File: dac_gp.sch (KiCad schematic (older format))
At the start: 47 parts, among them U1 DAC80508ZRTER, U2 OPA2156xD, U26 OPA2156xD, U27 OPA2156xD, U28 OPA2156xD, U3 OPA2156xD, U4 OPA2156xD, U6 OPA2156xD, U7 TMUX6136PWR, U8 OPA2156xD, U9 TMUX6136PWR

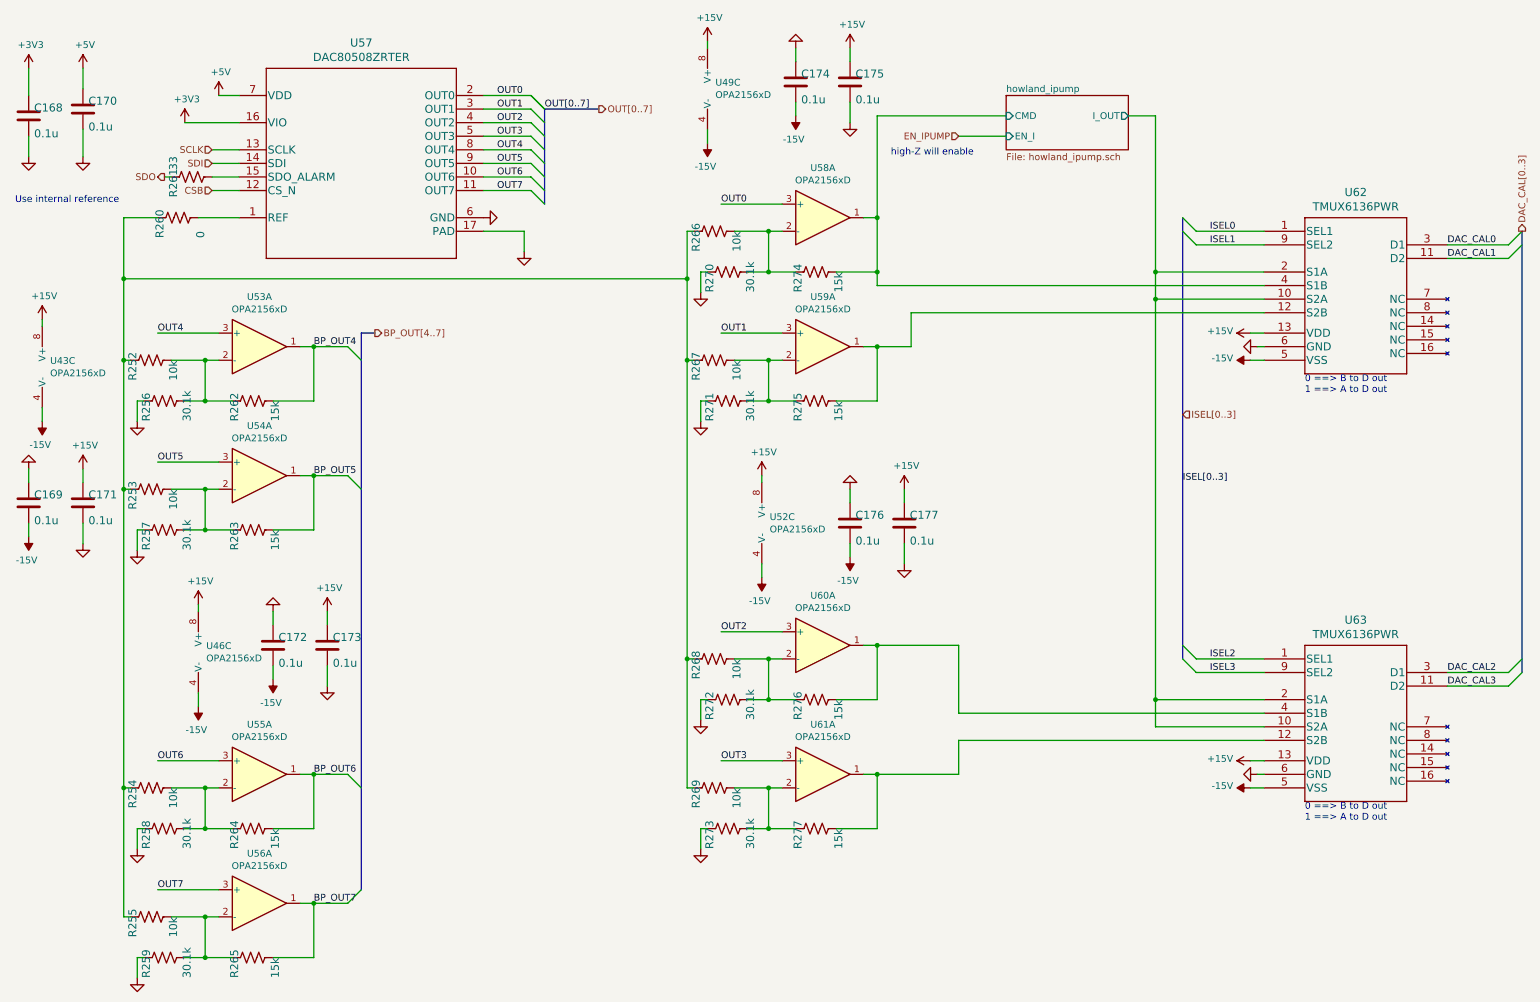
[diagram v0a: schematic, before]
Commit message: added Unique ID chip
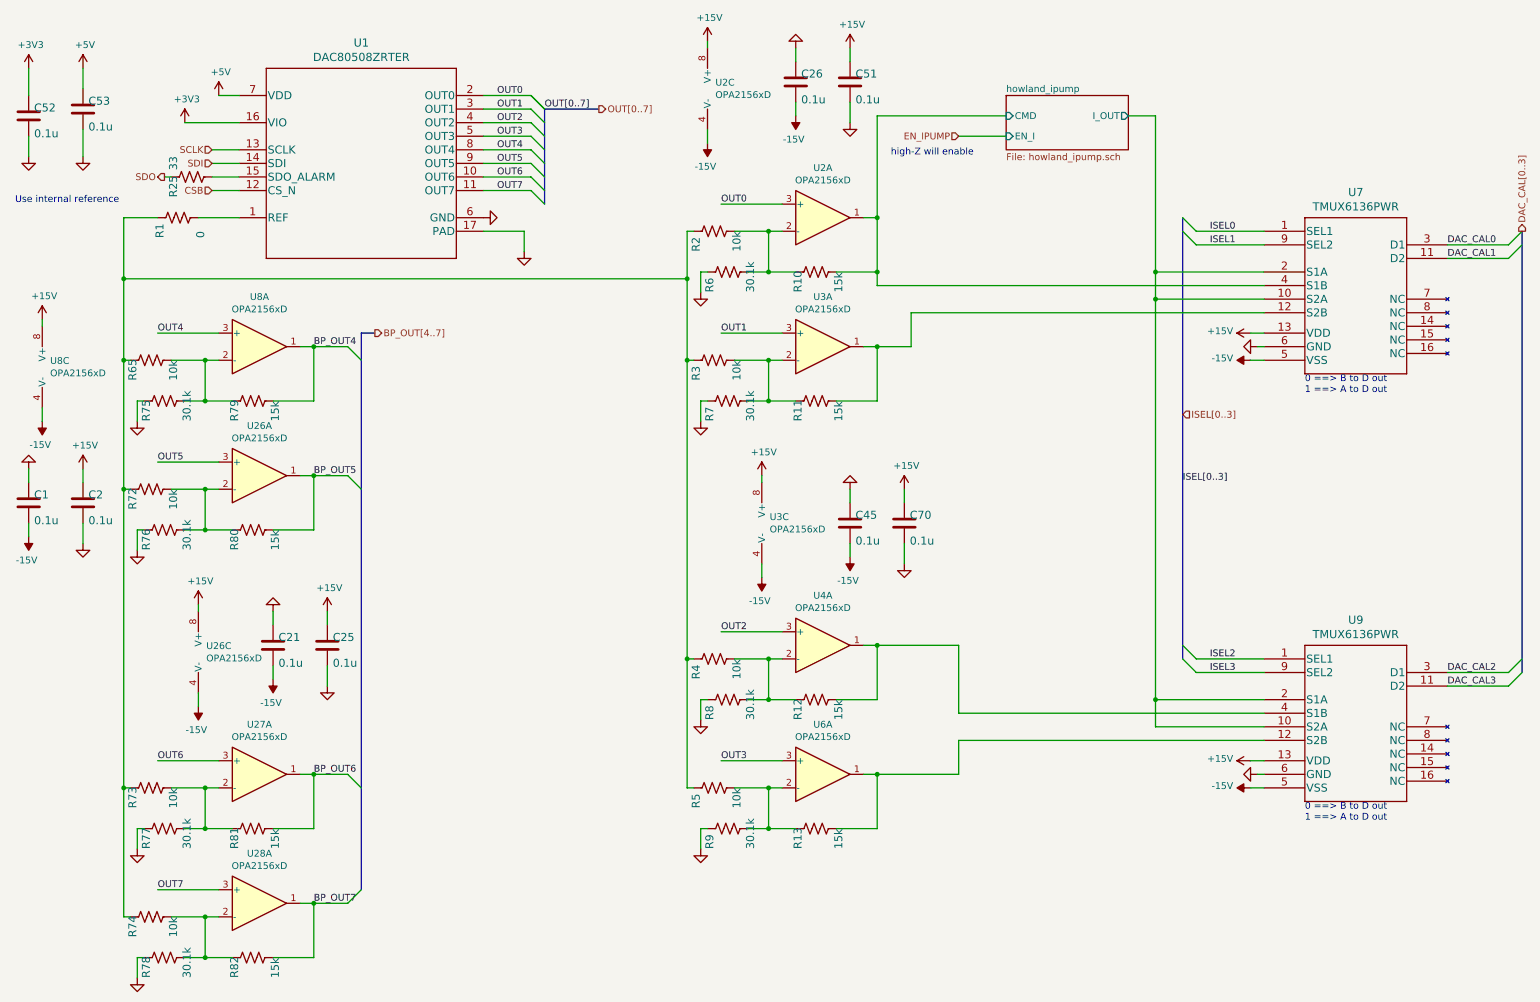
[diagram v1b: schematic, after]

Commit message: updates of DAC part placement
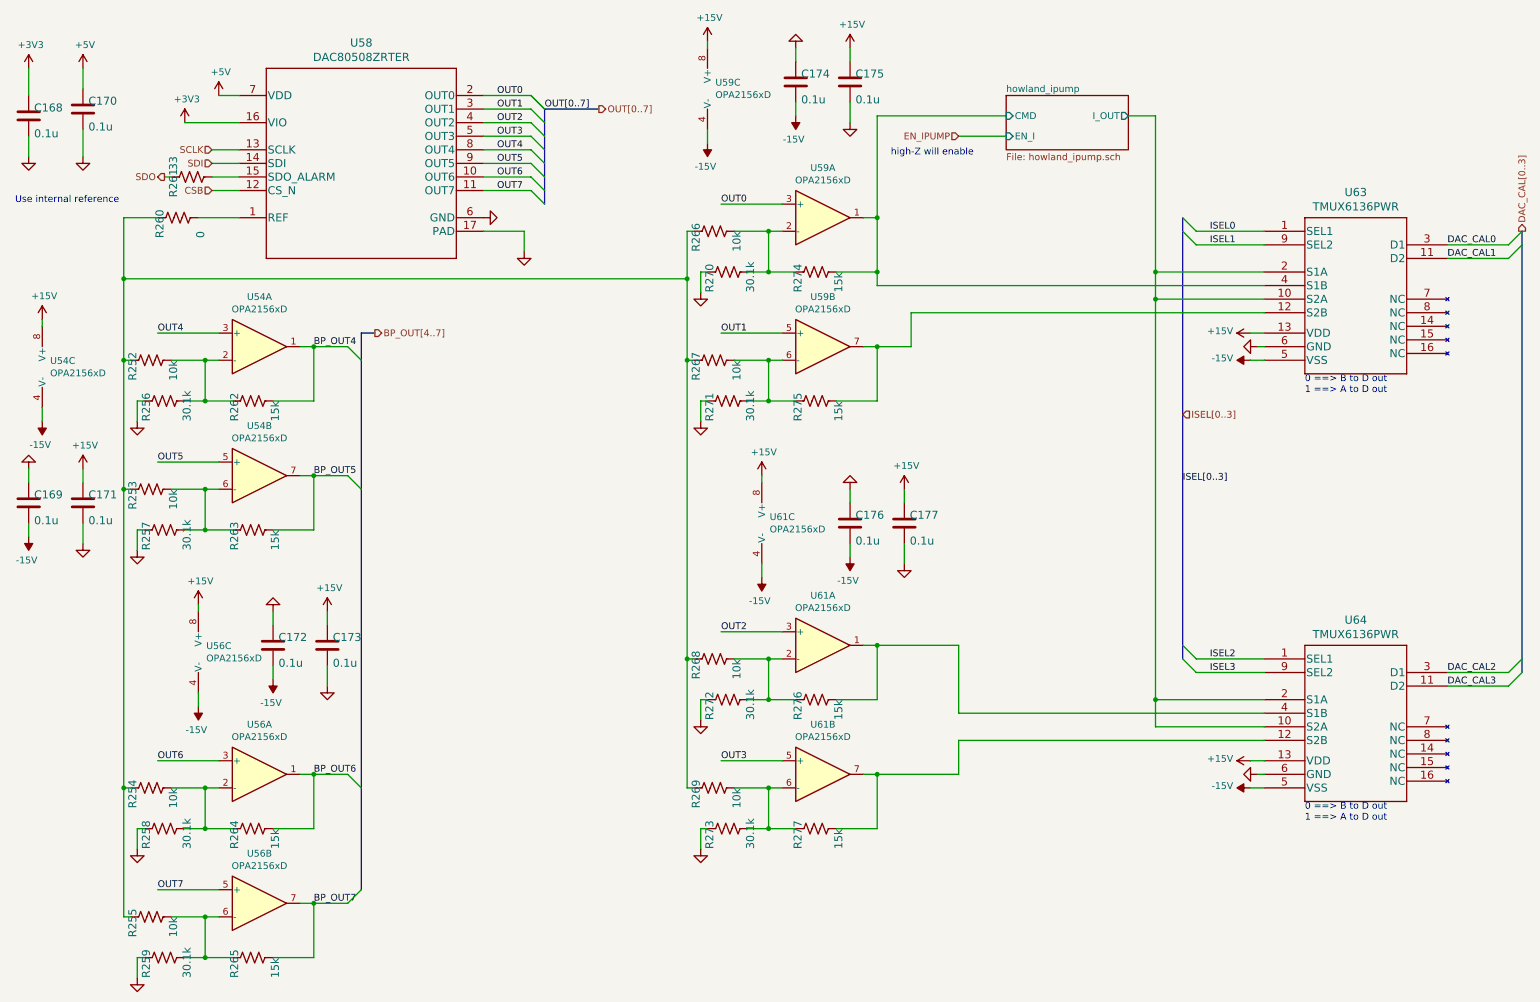
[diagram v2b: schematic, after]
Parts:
- renumbered C52 to C1, C70 to C10, C1 to C2, C53 to C3, C2 to C4, C21 to C5, C25 to C6, C26 to C7, C51 to C8, C45 to C9, R65 to R1, R25 to R10, R79 to R11, R80 to R12, R81 to R13, R82 to R14, R2 to R15, R3 to R16, R4 to R17, R5 to R18, R6 to R19, R72 to R2, R7 to R20, R8 to R21, R9 to R22, R10 to R23, R11 to R24, R12 to R25, R13 to R26, R73 to R3, R74 to R4, R75 to R5, R76 to R6, R77 to R7, R78 to R8, R1 to R9, U8 to U1, U7 to U10, U9 to U11, U26 to U2, U27 to U3, U28 to U4, U1 to U5, U2 to U6, U3 to U7, U4 to U8, U6 to U9
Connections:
- net BP_OUT5: now also U2.7; no longer U2.1
- net BP_OUT7: now also U4.7; no longer U4.1
- net OUT1: now also U7.5 (+); no longer U7.3 (+)
- net OUT3: now also U9.5 (+); no longer U9.3 (+)
- net OUT5: now also U2.5 (+); no longer U2.3 (+)
- net OUT7: now also U4.5 (+); no longer U4.3 (+)
- net at R24.2, U10.12 (S2B): now also U7.7; no longer U7.1
- net at R16.2, R20.2, R24.1: now also U7.6 (-); no longer U7.2 (-)
- net at R26.2, U11.12 (S2B): now also U9.7; no longer U9.1
- net at R18.2, R22.2, R26.1: now also U9.6 (-); no longer U9.2 (-)
- net at R12.1, R2.2, R6.2: now also U2.6 (-); no longer U2.2 (-)
- net at R14.1, R4.2, R8.2: now also U4.6 (-); no longer U4.2 (-)

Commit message: completing gp DAC layout
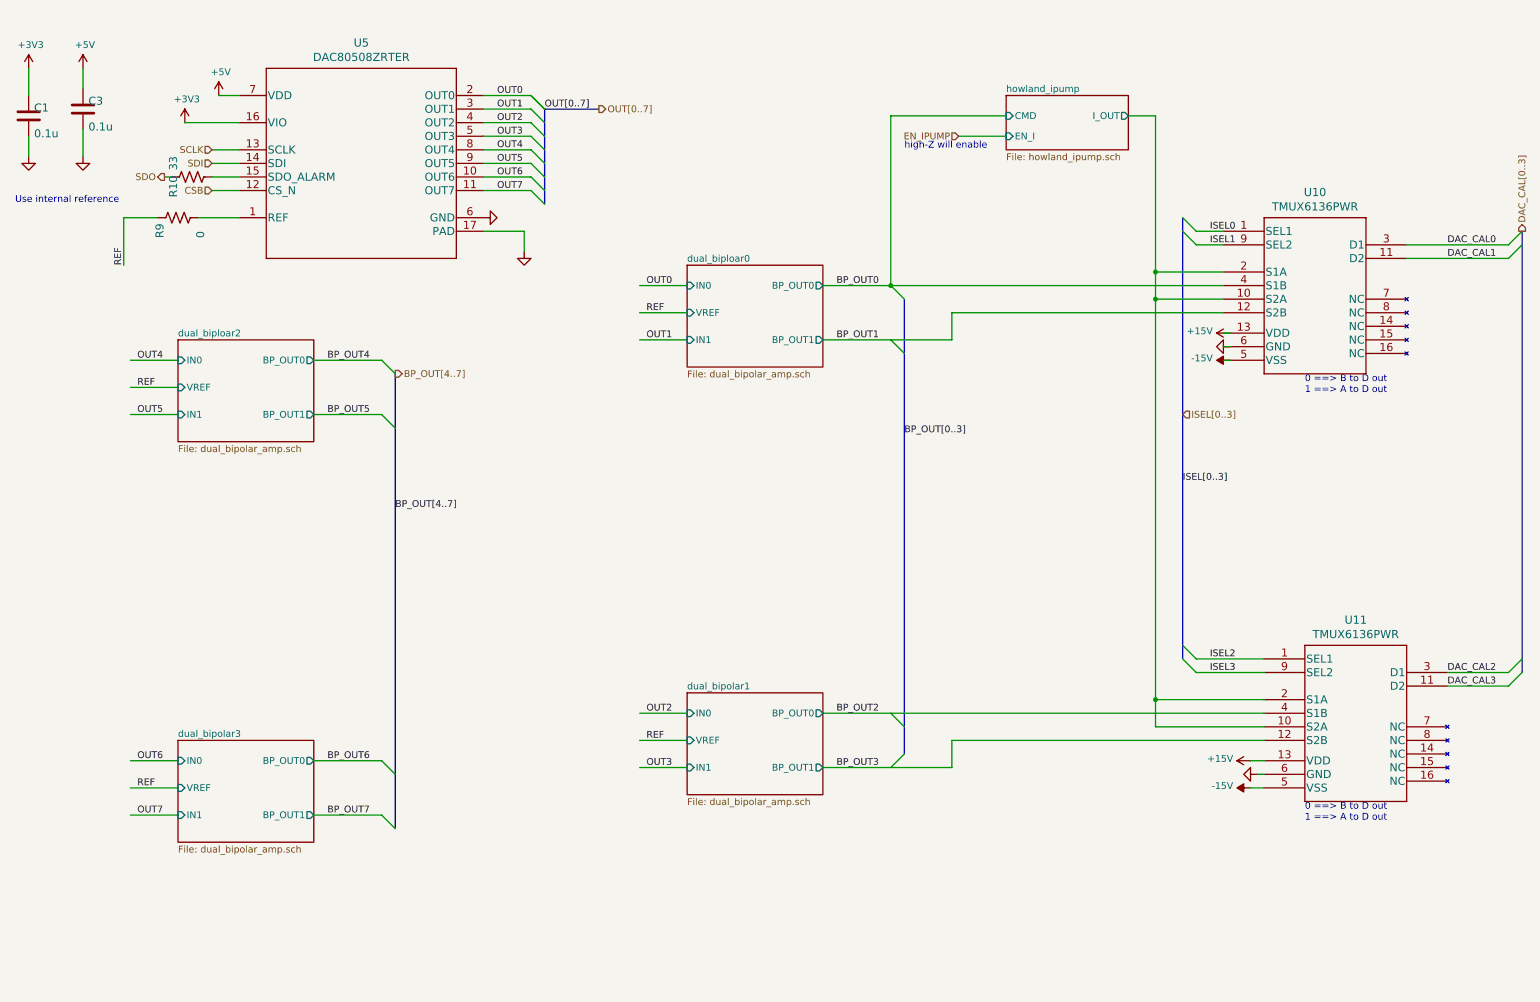
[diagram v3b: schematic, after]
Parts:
- removed C10, C2, C4, C5, C6, C7, C8, C9: 0.1u, Capacitor_SMD:C_0603_1608Metric, symbol Device:C
- removed R1, R15, R16, R17, R18, R2, R3, R4: 10k, Resistor_SMD:R_0603_1608Metric, symbol Device:R_US
- removed R11, R12, R13, R14, R23, R24, R25, R26: 15k, Resistor_SMD:R_0603_1608Metric, symbol Device:R_US
- removed R19, R20, R21, R22, R5, R6, R7, R8: 30.1k, Resistor_SMD:R_0603_1608Metric, symbol Device:R_US
- removed U1, U2, U3, U4, U6, U7, U8, U9: OPA2156xD, Package_SO:SOIC-8_3.9x4.9mm_P1.27mm, symbol Amplifier_Operational:OPA2156xD
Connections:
- net labels added: BP_OUT0, BP_OUT1, BP_OUT2, BP_OUT3, BP_OUT[0..3], REF
- wire segments 194 -> 75
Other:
- moved on the sheet: U10
